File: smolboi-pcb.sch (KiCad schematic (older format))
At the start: 113 parts, among them SW1 ESC, SW10 O, SW11 P, SW12 Bksp, SW13 Tab, SW14 A, SW15 S, SW16 D, SW17 F, SW18 G, SW19 H, SW2 Q, SW20 J, SW21 K, SW22 L, SW23 ;, SW24 ', SW25 Shift, SW26 Z, SW27 X, SW28 C, SW29 V, SW3 W, SW30 B, SW31 N, SW32 M, SW33 ,, SW34 ., SW35 /, SW36 CpsLk, SW37 Ctrl, SW38 Win, SW39 Alt, SW4 E, SW40 FUP, SW41 FDN, SW42 Space, SW43 FRI, SW44 Left, SW45 Del, SW46 Enter, SW48 SW_Push, SW5 R, SW6 T, SW7 Y, SW8 U, SW9 I, U1 STM32F103C8Tx, U2 PRTR5V0U2X, U3 XC6206, Y1 8MHz

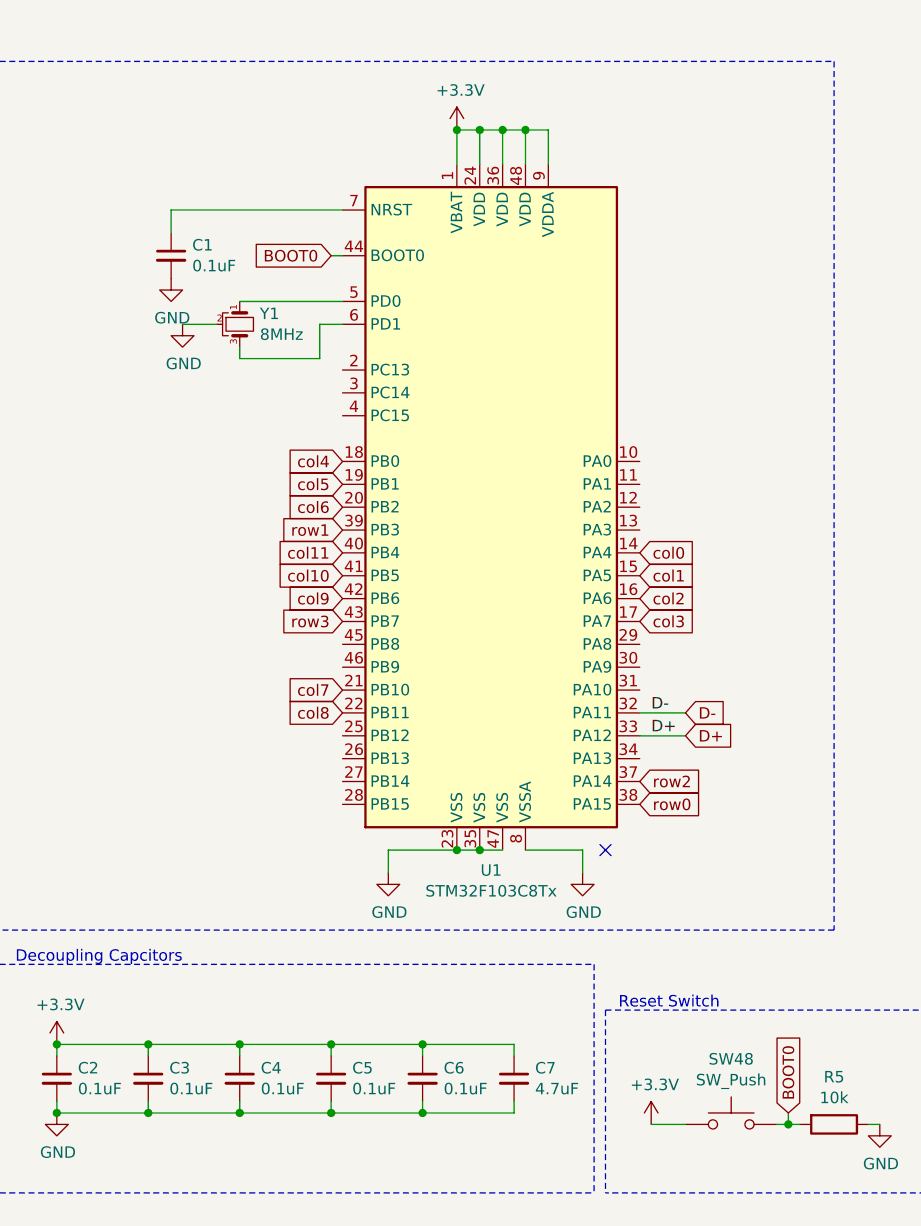
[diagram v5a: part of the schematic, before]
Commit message: replaced with STM32F072CBT6, rerouted
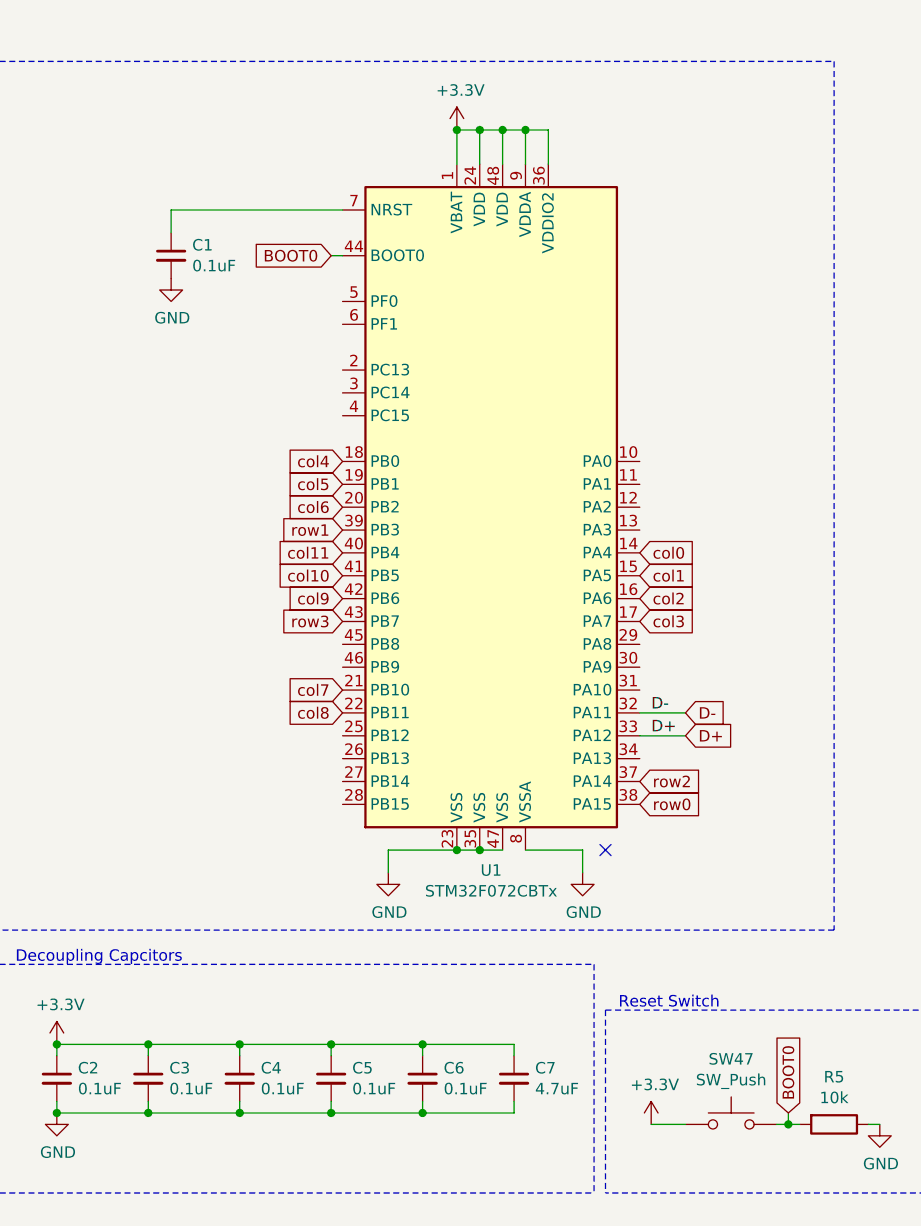
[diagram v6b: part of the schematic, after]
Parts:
- removed U1: STM32F103C8Tx, Package_QFP:LQFP-48_7x7mm_P0.5mm, symbol MCU_ST_STM32F1:STM32F103C8Tx
- removed Y1: 8MHz, CSTNE8M00GH5C000R0:OSC_CSTNE8M00GH5C000R0, symbol Device:Crystal_GND2_Small
- added U1: STM32F072CBTx, Package_QFP:LQFP-48_7x7mm_P0.5mm, symbol MCU_ST_STM32F0:STM32F072CBTx
- renumbered SW48 to SW47
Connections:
- net +3V3: now also U1.1 (VBAT), U1.24 (VDD), U1.36 (VDDIO2), U1.48 (VDD), U1.9 (VDDA)
- net BOOT0: now also U1.44 (BOOT0)
- net D+: now also U1.33 (PA12)
- net D-: now also U1.32 (PA11)
- net GND: now also U1.23 (VSS), U1.35 (VSS), U1.47 (VSS), U1.8 (VSSA)
- net col0: now also U1.14 (PA4)
- net col1: now also U1.15 (PA5)
- net col10: now also U1.41 (PB5)
- net col11: now also U1.40 (PB4)
- net col2: now also U1.16 (PA6)
- net col3: now also U1.17 (PA7)
- net col4: now also U1.18 (PB0)
- net col5: now also U1.19 (PB1)
- net col6: now also U1.20 (PB2)
- net col7: now also U1.21 (PB10)
- net col8: now also U1.22 (PB11)
- net col9: now also U1.42 (PB6)
- net row0: now also U1.38 (PA15)
- net row1: now also U1.39 (PB3)
- net row2: now also U1.37 (PA14)
- net row3: now also U1.43 (PB7)
- net at C1.1: now also U1.7 (NRST)
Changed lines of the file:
@@
-	1    0    0    -1
-$EndComp
-Wire Wire Line
-	2100 5350 2200 5350
-Wire Wire Line
-	2100 5500 2100 5350
-Wire Wire Line
-	1750 5500 2100 5500
-Wire Wire Line
-	1750 5450 1750 5500
-Wire Wire Line
-	1750 5250 2200 5250
-Wire Wire Line
-	1500 5350 1650 5350
-$Comp
-L Device:Crystal_GND2_Small Y1
-U 1 1 66AA59F8
-P 1750 5350
-F 0 "Y1" V 1704 5438 50  0000 L CNN
-F 1 "8MHz" V 1795 5438 50  0000 L CNN
-F 2 "CSTNE8M00GH5C000R0:OSC_CSTNE8M00GH5C000R0" H 1750 5350 50  0001 C CNN
-F 3 "~" H 1750 5350 50  0001 C CNN
-	1    1750 5350
-	0    1    1    0
-$EndComp
-$Comp
-L power:GND #PWR03
-U 1 1 66A960BE
-P 1500 5350
-F 0 "#PWR03" H 1500 5100 50  0001 C CNN
-F 1 "GND" H 1505 5177 50  0000 C CNN
-F 2 "" H 1500 5350 50  0001 C CNN
-F 3 "" H 1500 5350 50  0001 C CNN
-	1    1500 5350
 	1    0    0    -1
 $EndComp
@@
 Connection ~ 6150 8550
 $Comp
-L power:+3.3V #PWR012
+L power:+3.3V #PWR011
 U 1 1 669EBFC0
 P 6150 8550
-F 0 "#PWR012" H 6150 8400 50  0001 C CNN
+F 0 "#PWR011" H 6150 8400 50  0001 C CNN
 F 1 "+3.3V" H 6165 8723 50  0000 C CNN
 F 2 "" H 6150 8550 50  0001 C CNN
@@
 Connection ~ 5100 8550
 $Comp
-L power:+5V #PWR011
+L power:+5V #PWR010
 U 1 1 669EAEEE
 P 5100 8550
-F 0 "#PWR011" H 5100 8400 50  0001 C CNN
+F 0 "#PWR010" H 5100 8400 50  0001 C CNN
 F 1 "+5V" H 5115 8723 50  0000 C CNN
 F 2 "" H 5100 8550 50  0001 C CNN
@@
 $EndComp
 $Comp
-L power:GND #PWR016
+L power:GND #PWR015
 U 1 1 669E9A37
 P 5650 8850
-F 0 "#PWR016" H 5650 8600 50  0001 C CNN
+F 0 "#PWR015" H 5650 8600 50  0001 C CNN
 F 1 "GND" H 5655 8677 50  0000 C CNN
 F 2 "" H 5650 8850 50  0001 C CNN
@@
 	7900 7650 8000 7650
 $Comp
-L power:VCC #PWR07
+L power:VCC #PWR06
 U 1 1 66AEEB1B
 P 7300 7650
-F 0 "#PWR07" H 7300 7500 50  0001 C CNN
+F 0 "#PWR06" H 7300 7500 50  0001 C CNN
 F 1 "VCC" V 7318 7777 50  0000 L CNN
 F 2 "" H 7300 7650 50  0001 C CNN
@@
 Connection ~ 6400 6500
 $Comp
-L power:VCC #PWR04
+L power:VCC #PWR03
 U 1 1 66AED921
 P 6400 6500
-F 0 "#PWR04" H 6400 6350 50  0001 C CNN
+F 0 "#PWR03" H 6400 6350 50  0001 C CNN
 F 1 "VCC" H 6417 6673 50  0000 C CNN
 F 2 "" H 6400 6500 50  0001 C CNN
@@
 	5900 6500 6050 6500
 $Comp
-L power:+5V #PWR05
+L power:+5V #PWR04
 U 1 1 66A8F9EC
 P 7000 6500
-F 0 "#PWR05" H 7000 6350 50  0001 C CNN
+F 0 "#PWR04" H 7000 6350 50  0001 C CNN
 F 1 "+5V" H 7015 6673 50  0000 C CNN
 F 2 "" H 7000 6500 50  0001 C CNN
@@
 $EndComp
 $Comp
-L power:GND #PWR06
+L power:GND #PWR05
 U 1 1 66A8C4DF
 P 6100 7600
-F 0 "#PWR06" H 6100 7350 50  0001 C CNN
+F 0 "#PWR05" H 6100 7350 50  0001 C CNN
 F 1 "GND" H 6105 7427 50  0000 C CNN
 F 2 "" H 6100 7600 50  0001 C CNN
@@
 	3000 4500 3100 4500
 $Comp
-L power:GND #PWR09
+L power:GND #PWR08
 U 1 1 66A7C570
 P 3250 7750
-F 0 "#PWR09" H 3250 7500 50  0001 C CNN
+F 0 "#PWR08" H 3250 7500 50  0001 C CNN
 F 1 "GND" H 3255 7577 50  0000 C CNN
 F 2 "" H 3250 7750 50  0001 C CNN
@@
 	2400 7750 2400 7650
 $Comp
-L power:GND #PWR08
+L power:GND #PWR07
 U 1 1 66A7A626
 P 2400 7750
-F 0 "#PWR08" H 2400 7500 50  0001 C CNN
+F 0 "#PWR07" H 2400 7500 50  0001 C CNN
 F 1 "GND" H 2405 7577 50  0000 C CNN
 F 2 "" H 2400 7750 50  0001 C CNN
@@
 	4500 8850 4550 8850
 $Comp
-L power:GND #PWR015
+L power:GND #PWR014
 U 1 1 66A2731E
 P 4550 8850
-F 0 "#PWR015" H 4550 8600 50  0001 C CNN
+F 0 "#PWR014" H 4550 8600 50  0001 C CNN
 F 1 "GND" H 4555 8677 50  0000 C CNN
 F 2 "" H 4550 8850 50  0001 C CNN
@@
 	3550 8850 3700 8850
 $Comp
-L power:+3.3V #PWR014
+L power:+3.3V #PWR013
 U 1 1 66A25B4B
 P 3550 8850
-F 0 "#PWR014" H 3550 8700 50  0001 C CNN
+F 0 "#PWR013" H 3550 8700 50  0001 C CNN
 F 1 "+3.3V" H 3565 9023 50  0000 C CNN
 F 2 "" H 3550 8850 50  0001 C CNN
@@
 $EndComp
 $Comp
-L Switch:SW_Push SW48
+L Switch:SW_Push SW47
 U 1 1 66A24AC4
 P 3900 8850
-F 0 "SW48" H 3900 9135 50  0000 C CNN
+F 0 "SW47" H 3900 9135 50  0000 C CNN
 F 1 "SW_Push" H 3900 9044 50  0000 C CNN
 F 2 "Button_Switch_SMD:SW_SPST_SKQG_WithStem" H 3900 9050 50  0001 C CNN
@@
 NoConn ~ 3350 7650
 $Comp
-L power:+3.3V #PWR010
+L power:+3.3V #PWR09
 U 1 1 66A099A4
 P 950 8500
-F 0 "#PWR010" H 950 8350 50  0001 C CNN
+F 0 "#PWR09" H 950 8350 50  0001 C CNN
 F 1 "+3.3V" H 965 8673 50  0000 C CNN
 F 2 "" H 950 8500 50  0001 C CNN
@@
 $EndComp
 Connection ~ 2700 4500
-$Comp
-L MCU_ST_STM32F1:STM32F103C8Tx U1
-U 1 1 669C6B58
-P 2900 6150
-F 0 "U1" H 2850 4561 50  0000 C CNN
-F 1 "STM32F103C8Tx" H 2850 4470 50  0000 C CNN
-F 2 "Package_QFP:LQFP-48_7x7mm_P0.5mm" H 2300 4750 50  0001 R CNN
-F 3 "http://www.st.com/st-web-ui/static/active/en/resource/technical/document/datasheet/CD00161566.pdf" H 2900 6150 50  0001 C CNN
-	1    2900 6150
-	1    0    0    -1
-$EndComp
 Connection ~ 1350 8500
 Wire Wire Line
@@
 	950  8750 950  8800
 $Comp
-L power:GND #PWR013
+L power:GND #PWR012
 U 1 1 669DBBED
 P 950 8800
-F 0 "#PWR013" H 950 8550 50  0001 C CNN
+F 0 "#PWR012" H 950 8550 50  0001 C CNN
 F 1 "GND" H 955 8627 50  0000 C CNN
 F 2 "" H 950 8800 50  0001 C CNN
@@
 Text GLabel 2200 6050 0    50   Input ~ 0
 col5
+$Comp
+L MCU_ST_STM32F0:STM32F072CBTx U1
+U 1 1 66D9CF55
+P 2900 6150
+F 0 "U1" H 2850 4561 50  0000 C CNN
+F 1 "STM32F072CBTx" H 2850 4470 50  0000 C CNN
+F 2 "Package_QFP:LQFP-48_7x7mm_P0.5mm" H 2300 4750 50  0001 R CNN
+F 3 "http://www.st.com/st-web-ui/static/active/en/resource/technical/document/datasheet/DM00090510.pdf" H 2900 6150 50  0001 C CNN
+	1    2900 6150
+	1    0    0    -1
+$EndComp
 $EndSCHEMATC

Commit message: jlcpcb bom and pos files
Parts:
- C1, C2, C3, C4, C5, C6: LCSC (none) -> C307331
- C7: LCSC (none) -> C23733
- C8, C9: LCSC (none) -> C52923
- D1, D10, D11, D12, D13, D14, D15, D16, D17, D18, D19, D2, D20, D21, D22, D23, D24, D25, D26, D27, D28, D29, D3, D30, D31, D32, D33, D34, D35, D36, D37, D38, D39, D4, D40, D41, D42, D43, D44, D45, D46, D5, D6, D7, D8, D9: LCSC (none) -> C77978
- F1: LCSC (none) -> C70069
- R1, R2: LCSC (none) -> C6117666
- R3, R4: LCSC (none) -> C400635
- R5: LCSC (none) -> C850723
- SW47: LCSC (none) -> C115351
- U1: LCSC (none) -> C81720
- U2: LCSC (none) -> C12333
- U3: LCSC (none) -> C5446
- USB1: LCSC (none) -> C165948
